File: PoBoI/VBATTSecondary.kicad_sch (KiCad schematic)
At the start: 17 parts, among them Q10 SI5418DU-T1-GE3, Q11 SI7164DP-T1-GE3, U28 LTC4231IUD-2#TRPBF, U30 INA219AIDCNR

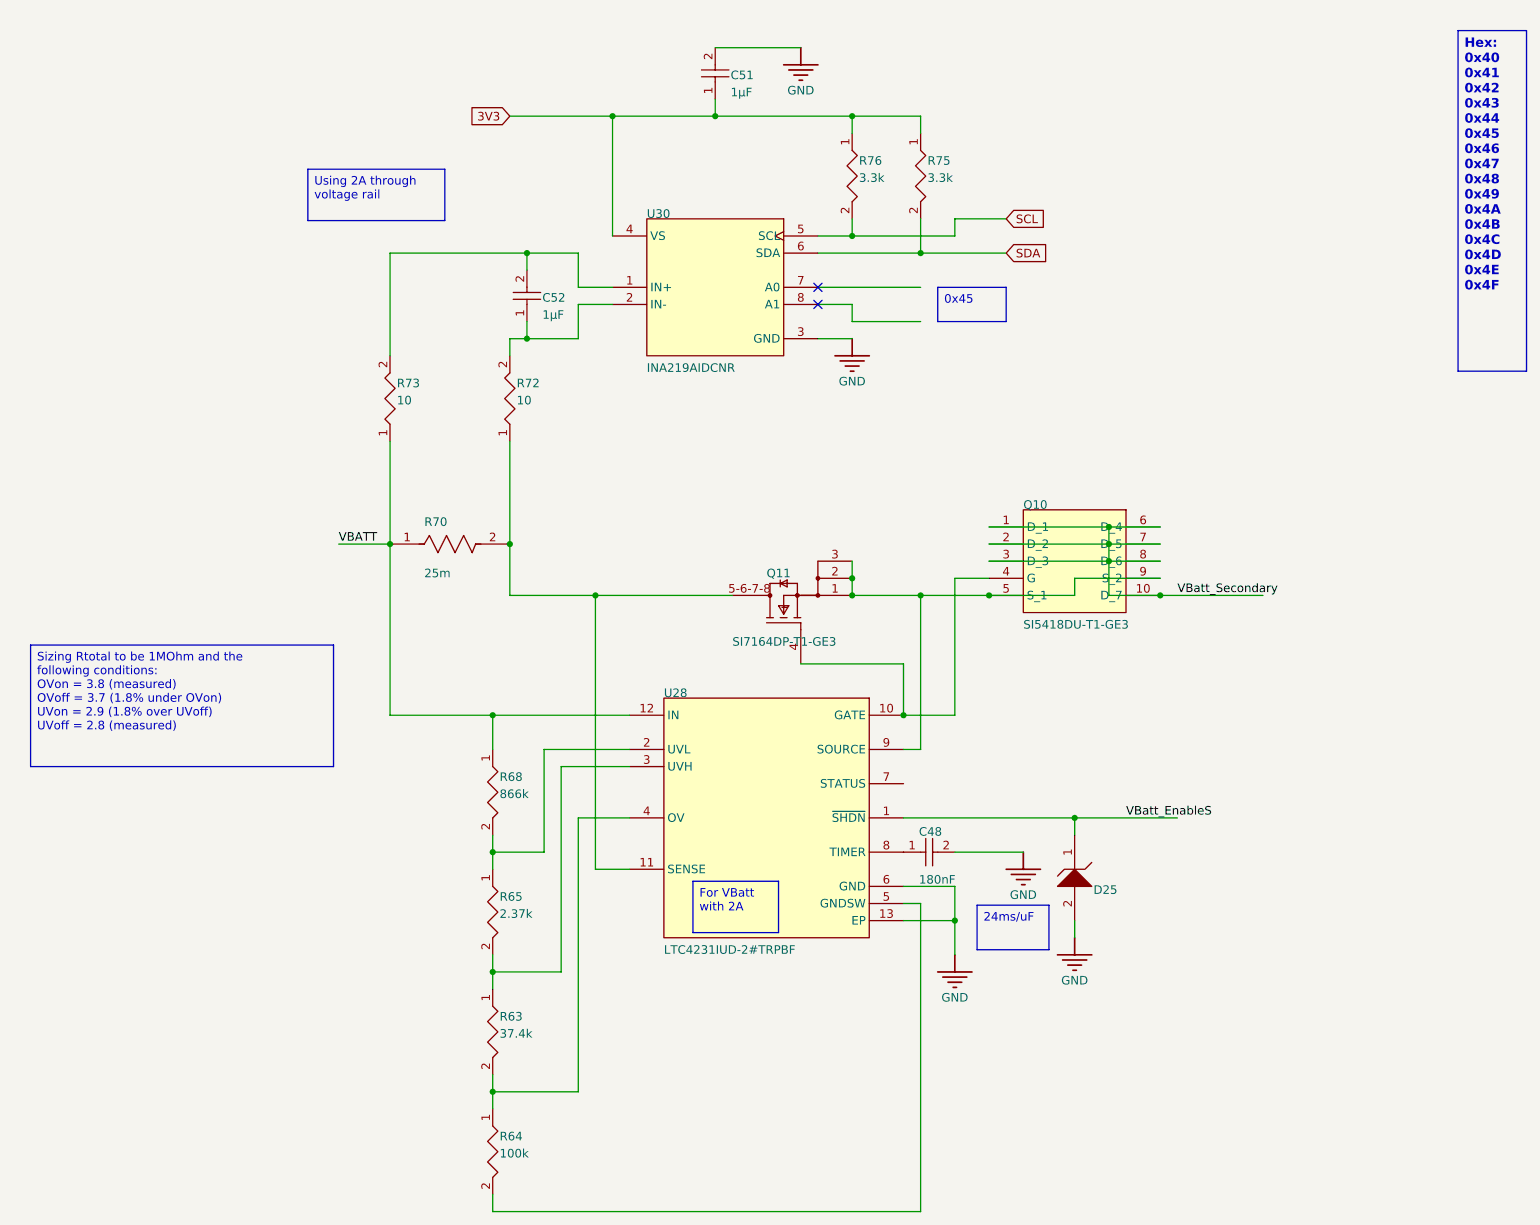
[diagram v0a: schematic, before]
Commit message: POBOI 4S updates: remove 12V/TVS sheets, fix VBATT dividers, INA219 addresses, U26
POBOI changes 10/28 Simon Ionashku

- Deleted the separate copy of the PCB file (BoardFix, it was an older version)
- Removed these sheets from the schematic and the board (no use for them anymore)
   - 12 PRIMARY
   - 12V BOOST
   - 12V SECONDARY
      - our 4S pack is already 12-16.8V so boosting to 12V does nothing, and the LM2622 is only rated for 12V in anyway
      - anything that needs ~12V can just use the VBATT Primary/Secondary rails
      - also deleted the "NEED TO ADD 12V COMPATIBILITY" note on the STM32 sheet
   - TVS_DIODES
      - they weren't actually connected to anything (cathodes were all no-connects)
      - they're also just 3.6V zeners, not real TVS diodes
      - the LTC4231 already shuts off on overvoltage, undervoltage and overcurrent, and there's a small zener clamp on each enable line
- Fixed the VBATT Primary and Secondary divider resistors since they were still using the 2S numbers and we moved to 4S
   - with the old values the switches would've never turned on (they cut off above ~8V)
   - new thresholds: OVoff = 17.5V, UVon = 12.4V, UVoff = 12.0V (3.0V per cell)
   - RES    OLD     NEW
      R71    866k    931k   (Primary)
      R74    2.37k   2.15k  (Primary)
      R77    37.4k   18.7k  (Primary)
      R78    100k    45.3k  (Primary)
      R68    866k    931k   (Secondary)
      R65    2.37k   2.15k  (Secondary)
      R63    37.4k   18.7k  (Secondary)
      R64    100k    45.3k  (Secondary)
   - updated the values, part numbers and form factor (all 0603 now) in the BOM and field table
      - R68/R71 were 0201 rated for 25V which is cutting it close at 16.8V
   - updated the notes and calculations on both sheets
- Fixed the INA219 addresses
   - a bunch of the A0/A1 pins were floating (marked no-connect) so the addresses would've been random
   - went through and checked/corrected all six so A0 and A1 match the slave address table
      5V Primary    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
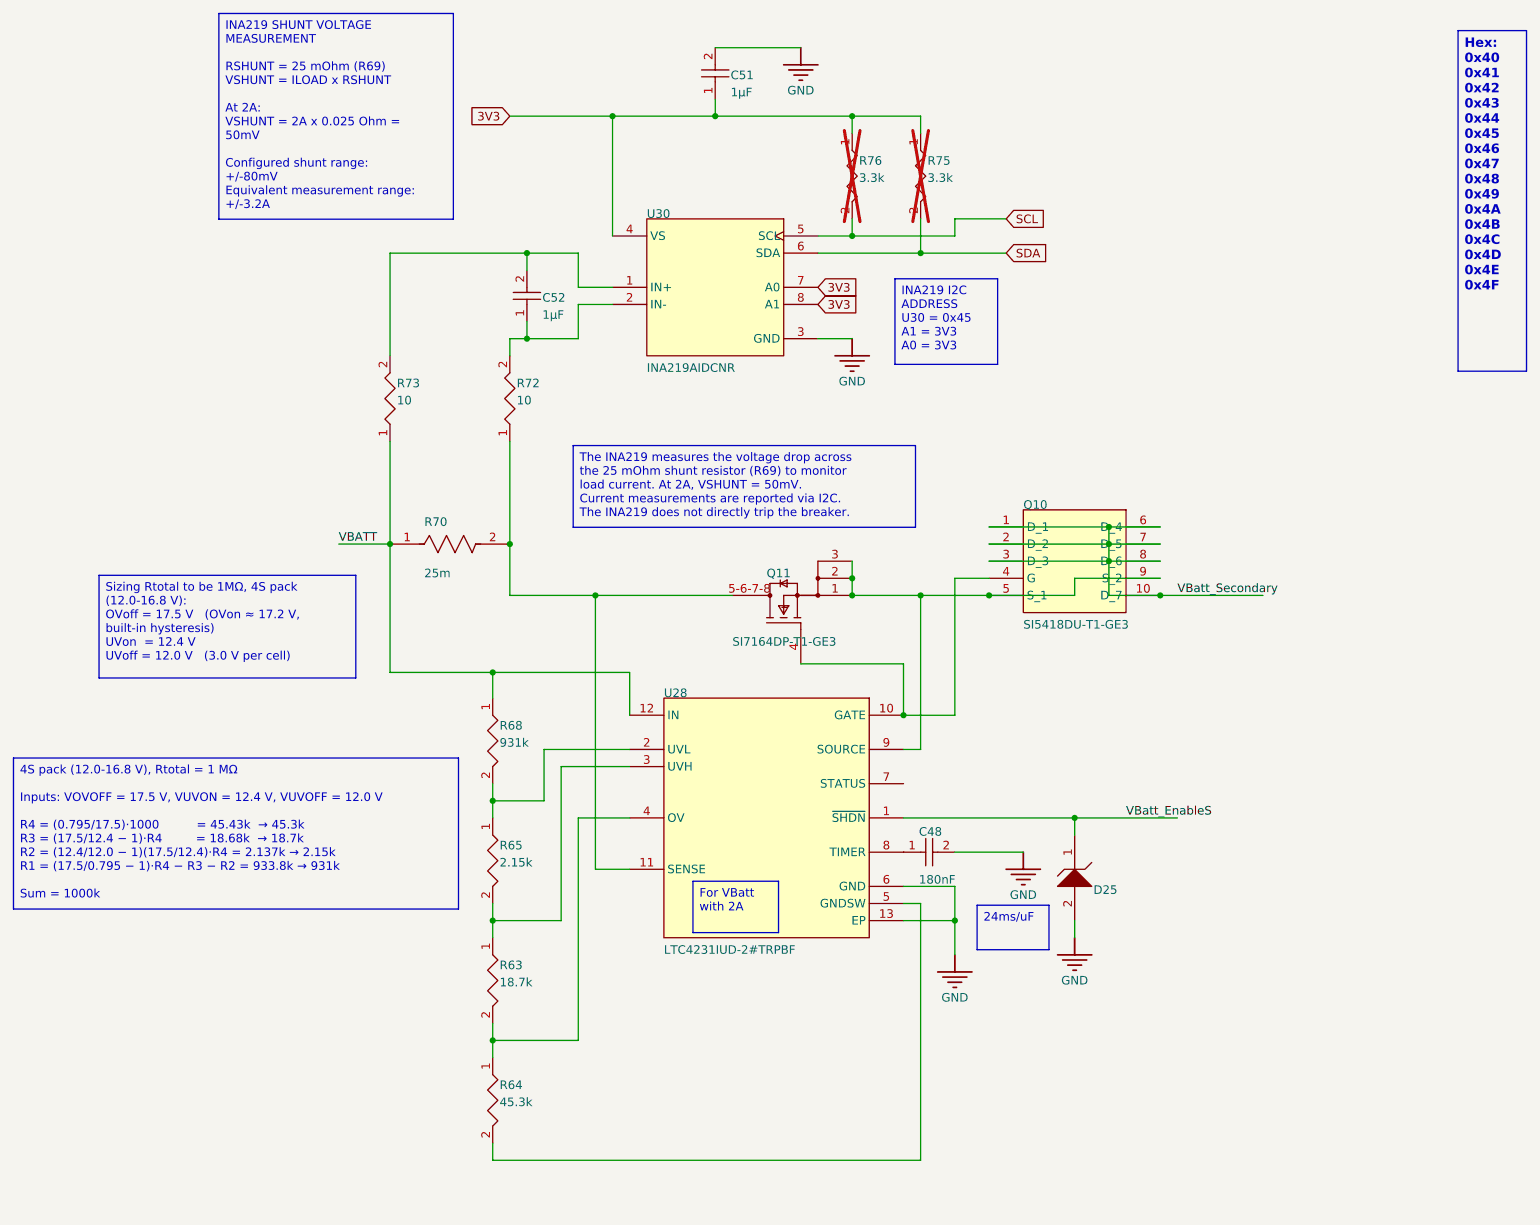
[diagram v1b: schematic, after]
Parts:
- R63: value CR0603-FX-3742ELF -> RC0603FR-0718K7L; ALTIUM_VALUE 37.4k -> 18.7k
- R64: value Resistor 100k +/-1% 0402 100 mW -> RC0603FR-0745K3L; footprint Vault:RESC1005X40X25ML05T05 -> Vault:RESC0603(1608)_L; ALTIUM_VALUE 100k -> 45.3k
- R65: value 2D37KR2F -> RC0603FR-072K15L; footprint Vault:RESC0402(1005)_L -> Vault:RESC0603(1608)_L; ALTIUM_VALUE 2.37k -> 2.15k
- R68: value MC0201L6F8663SE -> RC0603FR-07931KL; footprint Vault:RESC0603X26X15NL03T05 -> Vault:RESC0603(1608)_L; ALTIUM_VALUE 866k -> 931k
- R75, R76: now not fitted
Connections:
- net 3V3: now also U30.7 (A0), U30.8 (A1)
- no-connect marks 2 -> 0
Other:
- moved on the sheet: R63, R64, R65, R68
